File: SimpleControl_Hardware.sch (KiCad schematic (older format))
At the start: 29 parts, among them J1 Jack-DC, J2 AudioJack3, SW1 SW_SPDT, U1 MCP3208, U2 ProMicro, U3 CD74HC154M96, U4 MCP23017_SO

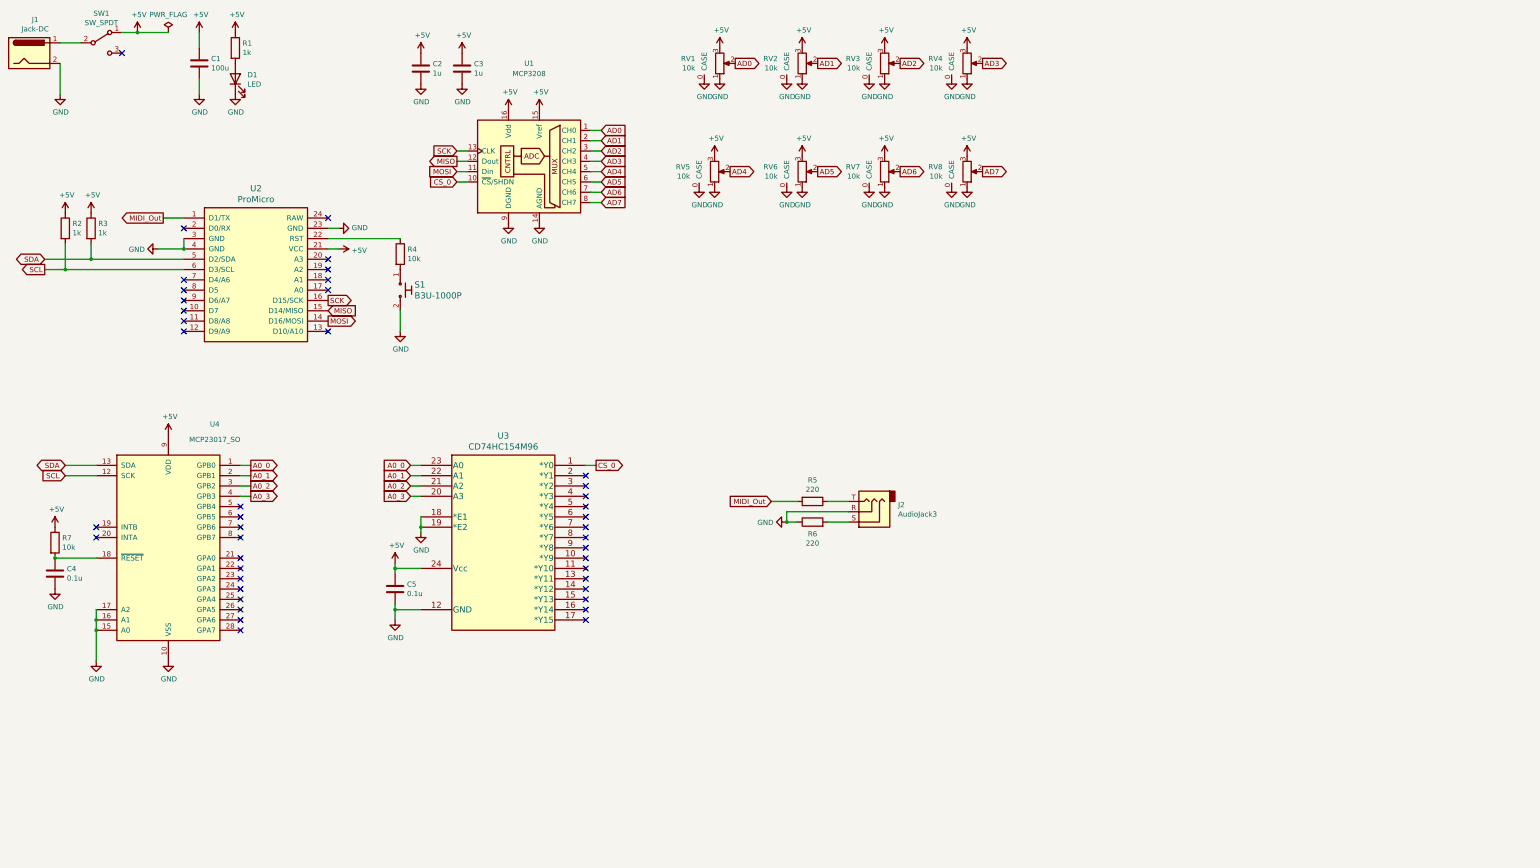
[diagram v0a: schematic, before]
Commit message: ADCのCSが1つにならない問題を修正しました。
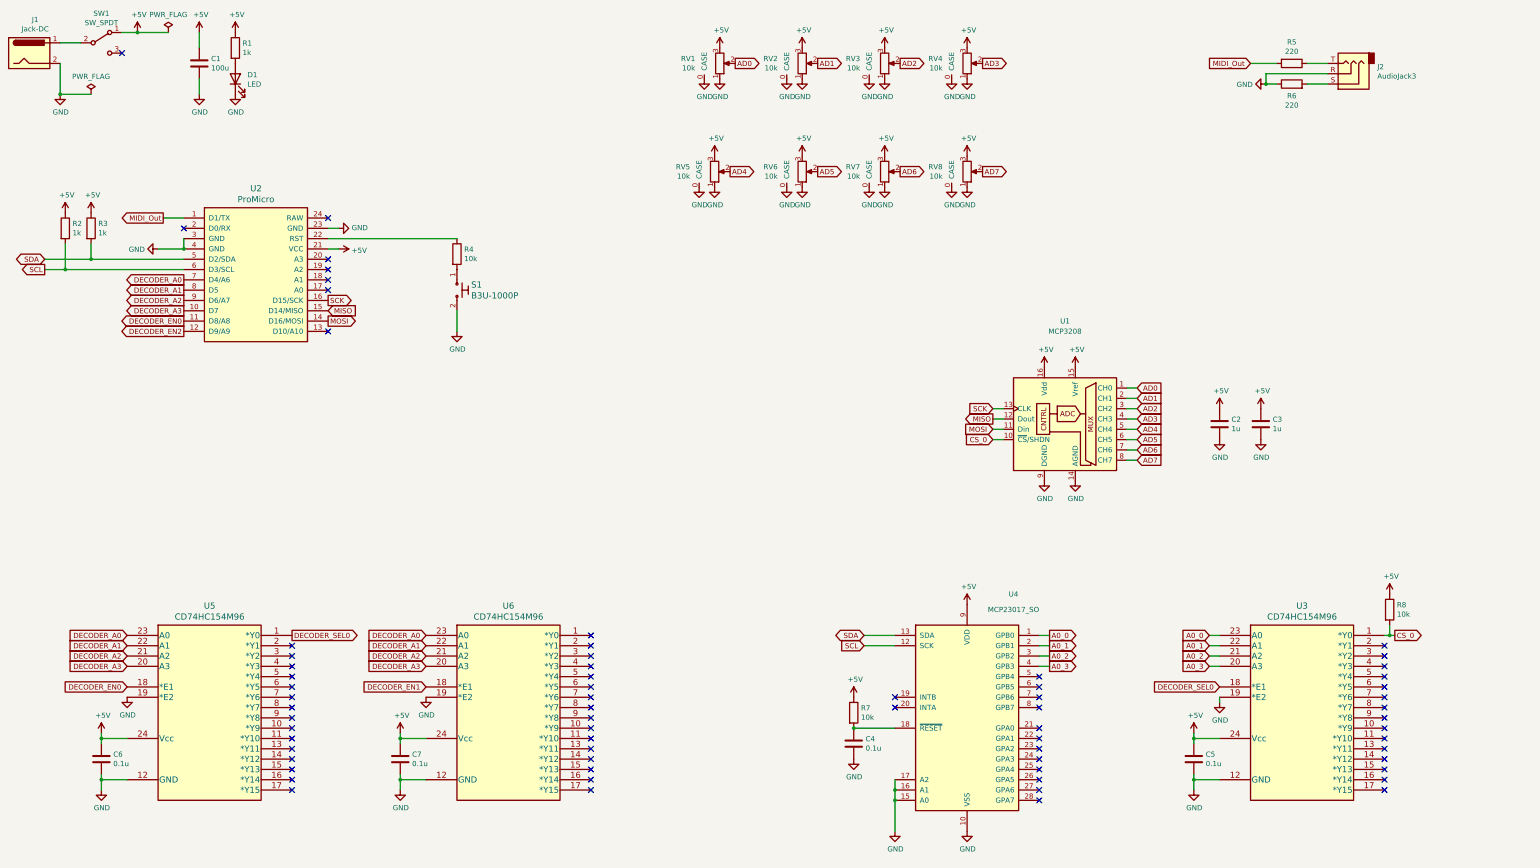
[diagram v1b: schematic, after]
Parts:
- added C6, C7: 0.1u, symbol Device:C
- added R8: 10k, symbol Device:R
- added U5, U6: CD74HC154M96, DW24, symbol SimpleControl:CD74HC154M96
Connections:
- net +5V: now also C6.1, C7.1, R8.1, U5.24 (Vcc), U6.24 (Vcc)
- net CS_0: now also R8.2
- net GND: now also C6.2, C7.2, U5.12 (GND), U5.19 (*E2), U6.12 (GND), U6.19 (*E2); no longer U3.18 (*E1)
- net DECODER_A3: now reaches U2.10 (D7)
- net DECODER_A3: now also U5.20 (A3), U6.20 (A3)
- net DECODER_EN0: now reaches U2.11 (D8/A8)
- net DECODER_EN0: now also U5.18 (*E1)
- net DECODER_EN2: now reaches U2.12 (D9/A9)
- net DECODER_A0: now reaches U2.7 (D4/A6)
- net DECODER_A0: now also U5.23 (A0), U6.23 (A0)
- net DECODER_A1: now reaches U2.8 (D5)
- net DECODER_A1: now also U5.22 (A1), U6.22 (A1)
- net DECODER_A2: now reaches U2.9 (D6/A7)
- net DECODER_A2: now also U5.21 (A2), U6.21 (A2)
- new net DECODER_EN1: U6.18 (*E1)
- new net DECODER_SEL0: U3.18 (*E1), U5.1 (*Y0)
- no-connect marks 43 -> 68
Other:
- moved on the sheet: C2, C3, C4, C5, J2, R4, R5, R6, R7, S1, U1, U3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

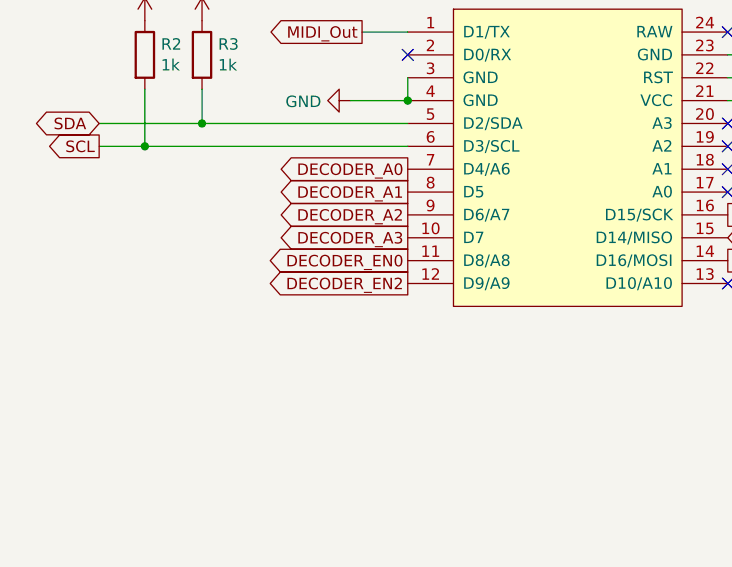
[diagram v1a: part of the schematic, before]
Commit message: add footprint info, generate netlist
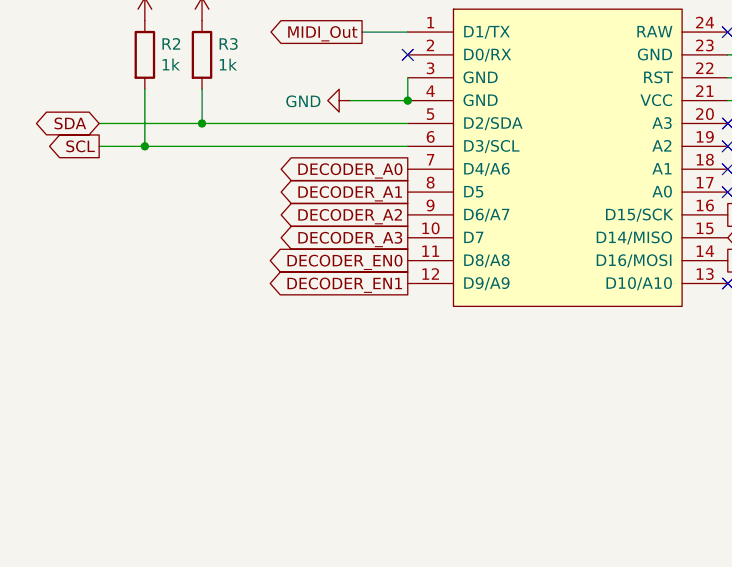
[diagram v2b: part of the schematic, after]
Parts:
- C1: footprint (none) -> Capacitors_SMD:C_1206_HandSoldering
- C2, C3, C4, C5, C6, C7: footprint (none) -> Capacitors_SMD:C_0603_HandSoldering
- D1: footprint (none) -> SimpleControl_Hardware:LED_0603_HandSoldering_easier
- J1: footprint (none) -> digikey:Barrel_Jack_5.5mmODx2.1mmID_PJ-202A
- J2: footprint (none) -> SimpleControl_Hardware:CUI_SJ-3523-SMT-TR
- R1, R2, R3, R4, R5, R6, R7, R8: footprint (none) -> Resistors_SMD:R_0603_HandSoldering
- RV1, RV2, RV3, RV4, RV5, RV6, RV7, RV8: footprint (none) -> SimpleControl_Hardware:Potentiometer_Alps_RK09K_Horizontal_CORRECTED
- SW1: footprint (none) -> SimpleControl_Hardware:SW_SPDT_2.5mm
- U1: footprint (none) -> Housings_SOIC:SOIC-14_3.9x8.7mm_Pitch1.27mm
- U2: footprint (none) -> SimpleControl_Hardware:ProMicro
- U3, U5, U6: footprint DW24 -> SimpleControl_Hardware:CD74HC154M96
- U4: footprint Package_SO:SOIC-28W_7.5x17.9mm_P1.27mm -> SimpleControl_Hardware:MCP23017_SO
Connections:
- net DECODER_EN2 is gone; now on net DECODER_EN1: U2.12 (D9/A9)
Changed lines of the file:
@@
 F 0 "U1" H 11200 5600 50  0000 C CNN
 F 1 "MCP3208" H 11200 5500 50  0000 C CNN
-F 2 "" H 11300 4750 50  0001 C CNN
+F 2 "Housings_SOIC:SOIC-14_3.9x8.7mm_Pitch1.27mm" H 11300 4750 50  0001 C CNN
 F 3 "http://ww1.microchip.com/downloads/en/DeviceDoc/21298c.pdf" H 11300 4750 50  0001 C CNN
 	1    11200 4650
@@
 F 0 "U2" H 3350 4487 60  0000 C CNN
 F 1 "ProMicro" H 3350 4381 60  0000 C CNN
-F 2 "" H 3450 2400 60  0000 C CNN
+F 2 "SimpleControl_Hardware:ProMicro" H 3450 2400 60  0001 C CNN
 F 3 "" H 3450 2400 60  0000 C CNN
 	1    3350 3450
@@
 F 0 "J1" H 1207 1425 50  0000 C CNN
 F 1 "Jack-DC" H 1207 1334 50  0000 C CNN
-F 2 "" H 1200 1060 50  0001 C CNN
+F 2 "digikey:Barrel_Jack_5.5mmODx2.1mmID_PJ-202A" H 1200 1060 50  0001 C CNN
 F 3 "~" H 1200 1060 50  0001 C CNN
 	1    1150 1100
@@
 F 0 "SW1" H 1850 1285 50  0000 C CNN
 F 1 "SW_SPDT" H 1850 1194 50  0000 C CNN
-F 2 "" H 1850 1000 50  0001 C CNN
+F 2 "SimpleControl_Hardware:SW_SPDT_2.5mm" H 1850 1000 50  0001 C CNN
 F 3 "~" H 1850 1000 50  0001 C CNN
 	1    1850 1000
@@
 F 0 "C1" H 2915 1246 50  0000 L CNN
 F 1 "100u" H 2915 1155 50  0000 L CNN
-F 2 "" H 2838 1050 50  0001 C CNN
+F 2 "Capacitors_SMD:C_1206_HandSoldering" H 2838 1050 50  0001 C CNN
 F 3 "~" H 2800 1200 50  0001 C CNN
 	1    2800 1200
@@
 F 0 "R1" H 3220 1096 50  0000 L CNN
 F 1 "1k" H 3220 1005 50  0000 L CNN
-F 2 "" V 3080 1050 50  0001 C CNN
+F 2 "Resistors_SMD:R_0603_HandSoldering" V 3080 1050 50  0001 C CNN
 F 3 "~" H 3150 1050 50  0001 C CNN
 	1    3150 1050
@@
 F 0 "D1" V 3189 1233 50  0000 R CNN
 F 1 "LED" V 3098 1233 50  0000 R CNN
-F 2 "" H 3150 1350 50  0001 C CNN
+F 2 "SimpleControl_Hardware:LED_0603_HandSoldering_easier" H 3150 1350 50  0001 C CNN
 F 3 "~" H 3150 1350 50  0001 C CNN
 	1    3150 1350
@@
 F 0 "U4" H 10700 8750 50  0000 C CNN
 F 1 "MCP23017_SO" H 10700 8600 50  0000 C CNN
-F 2 "Package_SO:SOIC-28W_7.5x17.9mm_P1.27mm" H 10450 6550 50  0001 L CNN
+F 2 "SimpleControl_Hardware:MCP23017_SO" H 10450 6550 50  0001 L CNN
 F 3 "http://ww1.microchip.com/downloads/en/DeviceDoc/20001952C.pdf" H 10450 6450 50  0001 L CNN
 	1    10250 7550
@@
 F 0 "R3" H 1820 2846 50  0000 L CNN
 F 1 "1k" H 1820 2755 50  0000 L CNN
-F 2 "" V 1680 2800 50  0001 C CNN
+F 2 "Resistors_SMD:R_0603_HandSoldering" V 1680 2800 50  0001 C CNN
 F 3 "~" H 1750 2800 50  0001 C CNN
 	1    1750 2800
@@
 F 0 "R2" H 1570 2846 50  0000 L CNN
 F 1 "1k" H 1570 2755 50  0000 L CNN
-F 2 "" V 1430 2800 50  0001 C CNN
+F 2 "Resistors_SMD:R_0603_HandSoldering" V 1430 2800 50  0001 C CNN
 F 3 "~" H 1500 2800 50  0001 C CNN
 	1    1500 2800
@@
 F 0 "R5" V 13193 1200 50  0000 C CNN
 F 1 "220" V 13284 1200 50  0000 C CNN
-F 2 "" V 13330 1200 50  0001 C CNN
+F 2 "Resistors_SMD:R_0603_HandSoldering" V 13330 1200 50  0001 C CNN
 F 3 "~" H 13400 1200 50  0001 C CNN
 	1    13400 1200
@@
 F 0 "J2" H 13670 1233 50  0000 R CNN
 F 1 "AudioJack3" H 13670 1324 50  0000 R CNN
-F 2 "" H 13950 1300 50  0001 C CNN
+F 2 "SimpleControl_Hardware:CUI_SJ-3523-SMT-TR" H 13950 1300 50  0001 C CNN
 F 3 "~" H 13950 1300 50  0001 C CNN
 	1    13950 1300
@@
 F 0 "R6" V 13285 1400 50  0000 C CNN
 F 1 "220" V 13194 1400 50  0000 C CNN
-F 2 "" V 13330 1400 50  0001 C CNN
+F 2 "Resistors_SMD:R_0603_HandSoldering" V 13330 1400 50  0001 C CNN
 F 3 "~" H 13400 1400 50  0001 C CNN
 	1    13400 1400
@@
 F 0 "C4" H 9265 7846 50  0000 L CNN
 F 1 "0.1u" H 9265 7755 50  0000 L CNN
-F 2 "" H 9188 7650 50  0001 C CNN
+F 2 "Capacitors_SMD:C_0603_HandSoldering" H 9188 7650 50  0001 C CNN
 F 3 "~" H 9150 7800 50  0001 C CNN
 	1    9150 7800
@@
 F 0 "R7" H 9220 7546 50  0000 L CNN
 F 1 "10k" H 9220 7455 50  0000 L CNN
-F 2 "" V 9080 7500 50  0001 C CNN
+F 2 "Resistors_SMD:R_0603_HandSoldering" V 9080 7500 50  0001 C CNN
 F 3 "~" H 9150 7500 50  0001 C CNN
 	1    9150 7500
@@
 F 0 "C2" H 12815 4746 50  0000 L CNN
 F 1 "1u" H 12815 4655 50  0000 L CNN
-F 2 "" H 12738 4550 50  0001 C CNN
+F 2 "Capacitors_SMD:C_0603_HandSoldering" H 12738 4550 50  0001 C CNN
 F 3 "~" H 12700 4700 50  0001 C CNN
 	1    12700 4700
@@
 F 0 "C3" H 13215 4746 50  0000 L CNN
 F 1 "1u" H 13215 4655 50  0000 L CNN
-F 2 "" H 13138 4550 50  0001 C CNN
+F 2 "Capacitors_SMD:C_0603_HandSoldering" H 13138 4550 50  0001 C CNN
 F 3 "~" H 13100 4700 50  0001 C CNN
 	1    13100 4700
@@
 F 0 "R4" H 5370 3096 50  0000 L CNN
 F 1 "10k" H 5370 3005 50  0000 L CNN
-F 2 "" V 5230 3050 50  0001 C CNN
+F 2 "Resistors_SMD:R_0603_HandSoldering" V 5230 3050 50  0001 C CNN
 F 3 "~" H 5300 3050 50  0001 C CNN
 	1    5300 3050
@@
 F 0 "RV1" H 7612 1154 50  0000 R CNN
 F 1 "10k" H 7612 1245 50  0000 R CNN
-F 2 "" H 7850 1200 50  0001 C CNN
+F 2 "SimpleControl_Hardware:Potentiometer_Alps_RK09K_Horizontal_CORRECTED" H 7850 1200 50  0001 C CNN
 F 3 "~" H 7850 1200 50  0001 C CNN
 	1    7850 1200
@@
 F 0 "RV2" H 8412 1154 50  0000 R CNN
 F 1 "10k" H 8412 1245 50  0000 R CNN
-F 2 "" H 8650 1200 50  0001 C CNN
+F 2 "SimpleControl_Hardware:Potentiometer_Alps_RK09K_Horizontal_CORRECTED" H 8650 1200 50  0001 C CNN
 F 3 "~" H 8650 1200 50  0001 C CNN
 	1    8650 1200
@@
 F 0 "RV3" H 9212 1154 50  0000 R CNN
 F 1 "10k" H 9212 1245 50  0000 R CNN
-F 2 "" H 9450 1200 50  0001 C CNN
+F 2 "SimpleControl_Hardware:Potentiometer_Alps_RK09K_Horizontal_CORRECTED" H 9450 1200 50  0001 C CNN
 F 3 "~" H 9450 1200 50  0001 C CNN
 	1    9450 1200
@@
 F 0 "RV4" H 10012 1154 50  0000 R CNN
 F 1 "10k" H 10012 1245 50  0000 R CNN
-F 2 "" H 10250 1200 50  0001 C CNN
+F 2 "SimpleControl_Hardware:Potentiometer_Alps_RK09K_Horizontal_CORRECTED" H 10250 1200 50  0001 C CNN
 F 3 "~" H 10250 1200 50  0001 C CNN
 	1    10250 1200
@@
 F 0 "RV5" H 7562 2204 50  0000 R CNN
 F 1 "10k" H 7562 2295 50  0000 R CNN
-F 2 "" H 7800 2250 50  0001 C CNN
+F 2 "SimpleControl_Hardware:Potentiometer_Alps_RK09K_Horizontal_CORRECTED" H 7800 2250 50  0001 C CNN
 F 3 "~" H 7800 2250 50  0001 C CNN
 	1    7800 2250
@@
 F 0 "RV6" H 8412 2204 50  0000 R CNN
 F 1 "10k" H 8412 2295 50  0000 R CNN
-F 2 "" H 8650 2250 50  0001 C CNN
+F 2 "SimpleControl_Hardware:Potentiometer_Alps_RK09K_Horizontal_CORRECTED" H 8650 2250 50  0001 C CNN
 F 3 "~" H 8650 2250 50  0001 C CNN
 	1    8650 2250
@@
 F 0 "RV7" H 9212 2204 50  0000 R CNN
 F 1 "10k" H 9212 2295 50  0000 R CNN
-F 2 "" H 9450 2250 50  0001 C CNN
+F 2 "SimpleControl_Hardware:Potentiometer_Alps_RK09K_Horizontal_CORRECTED" H 9450 2250 50  0001 C CNN
 F 3 "~" H 9450 2250 50  0001 C CNN
 	1    9450 2250
@@
 F 0 "RV8" H 10012 2204 50  0000 R CNN
 F 1 "10k" H 10012 2295 50  0000 R CNN
-F 2 "" H 10250 2250 50  0001 C CNN
+F 2 "SimpleControl_Hardware:Potentiometer_Alps_RK09K_Horizontal_CORRECTED" H 10250 2250 50  0001 C CNN
 F 3 "~" H 10250 2250 50  0001 C CNN
 	1    10250 2250
@@
 F 0 "U3" H 13500 7237 60  0000 C CNN
 F 1 "CD74HC154M96" H 13500 7131 60  0000 C CNN
-F 2 "DW24" H 13500 7190 60  0001 C CNN
+F 2 "SimpleControl_Hardware:CD74HC154M96" H 13500 7190 60  0001 C CNN
 F 3 "" H 12700 6850 60  0000 C CNN
 	1    12700 6850
@@
 DECODER_EN0
 Text GLabel 2650 3800 0    50   Output ~ 0
-DECODER_EN2
+DECODER_EN1
 Text GLabel 2100 6750 0    50   Input ~ 0
 DECODER_A0
@@
 F 0 "C5" H 12565 7996 50  0000 L CNN
 F 1 "0.1u" H 12565 7905 50  0000 L CNN
-F 2 "" H 12488 7800 50  0001 C CNN
+F 2 "Capacitors_SMD:C_0603_HandSoldering" H 12488 7800 50  0001 C CNN
 F 3 "~" H 12450 7950 50  0001 C CNN
 	1    12450 7950
@@
 F 0 "C6" H 1965 7996 50  0000 L CNN
 F 1 "0.1u" H 1965 7905 50  0000 L CNN
-F 2 "" H 1888 7800 50  0001 C CNN
+F 2 "Capacitors_SMD:C_0603_HandSoldering" H 1888 7800 50  0001 C CNN
 F 3 "~" H 1850 7950 50  0001 C CNN
 	1    1850 7950
@@
 F 0 "C7" H 4865 7996 50  0000 L CNN
 F 1 "0.1u" H 4865 7905 50  0000 L CNN
-F 2 "" H 4788 7800 50  0001 C CNN
+F 2 "Capacitors_SMD:C_0603_HandSoldering" H 4788 7800 50  0001 C CNN
 F 3 "~" H 4750 7950 50  0001 C CNN
 	1    4750 7950
@@
 F 0 "U5" H 2900 7237 60  0000 C CNN
 F 1 "CD74HC154M96" H 2900 7131 60  0000 C CNN
-F 2 "DW24" H 2900 7190 60  0001 C CNN
+F 2 "SimpleControl_Hardware:CD74HC154M96" H 2900 7190 60  0001 C CNN
 F 3 "" H 2100 6850 60  0000 C CNN
 	1    2100 6850
@@
 F 0 "U6" H 5800 7237 60  0000 C CNN
 F 1 "CD74HC154M96" H 5800 7131 60  0000 C CNN
-F 2 "DW24" H 5800 7190 60  0001 C CNN
+F 2 "SimpleControl_Hardware:CD74HC154M96" H 5800 7190 60  0001 C CNN
 F 3 "" H 5000 6850 60  0000 C CNN
 	1    5000 6850
@@
 F 0 "R8" H 14420 6546 50  0000 L CNN
 F 1 "10k" H 14420 6455 50  0000 L CNN
-F 2 "" V 14280 6500 50  0001 C CNN
+F 2 "Resistors_SMD:R_0603_HandSoldering" V 14280 6500 50  0001 C CNN
 F 3 "~" H 14350 6500 50  0001 C CNN
 	1    14350 6500
@@
 $EndComp
 $Comp
-L power:PWR_FLAG #FLG?
+L power:PWR_FLAG #FLG0101
 U 1 1 5DF6AA2E
 P 1750 1500
-F 0 "#FLG?" H 1750 1575 50  0001 C CNN
+F 0 "#FLG0101" H 1750 1575 50  0001 C CNN
 F 1 "PWR_FLAG" H 1750 1673 50  0000 C CNN
 F 2 "" H 1750 1500 50  0001 C CNN
